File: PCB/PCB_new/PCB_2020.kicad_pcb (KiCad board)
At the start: 2 copper layers, 94 x 98.4 mm, 41 parts, among them IC1 LM358N, J1 SSW-110-02-G-S, J2 SSW-110-02-G-S, J3 SSW-110-02-G-S, J4 SSW-110-02-G-S, J5 SSW-110-02-G-S, J6 SSW-110-02-G-S, J7 SSW-110-02-G-S, J8 SSW-110-02-G-S, Q1 220mA/50V/3.5Ω, Q10 100V/17A, Q2 100V/17A, Q6 100V/17A, Q7 100V/17A, Q8 100V/17A, Q9 100V/17A

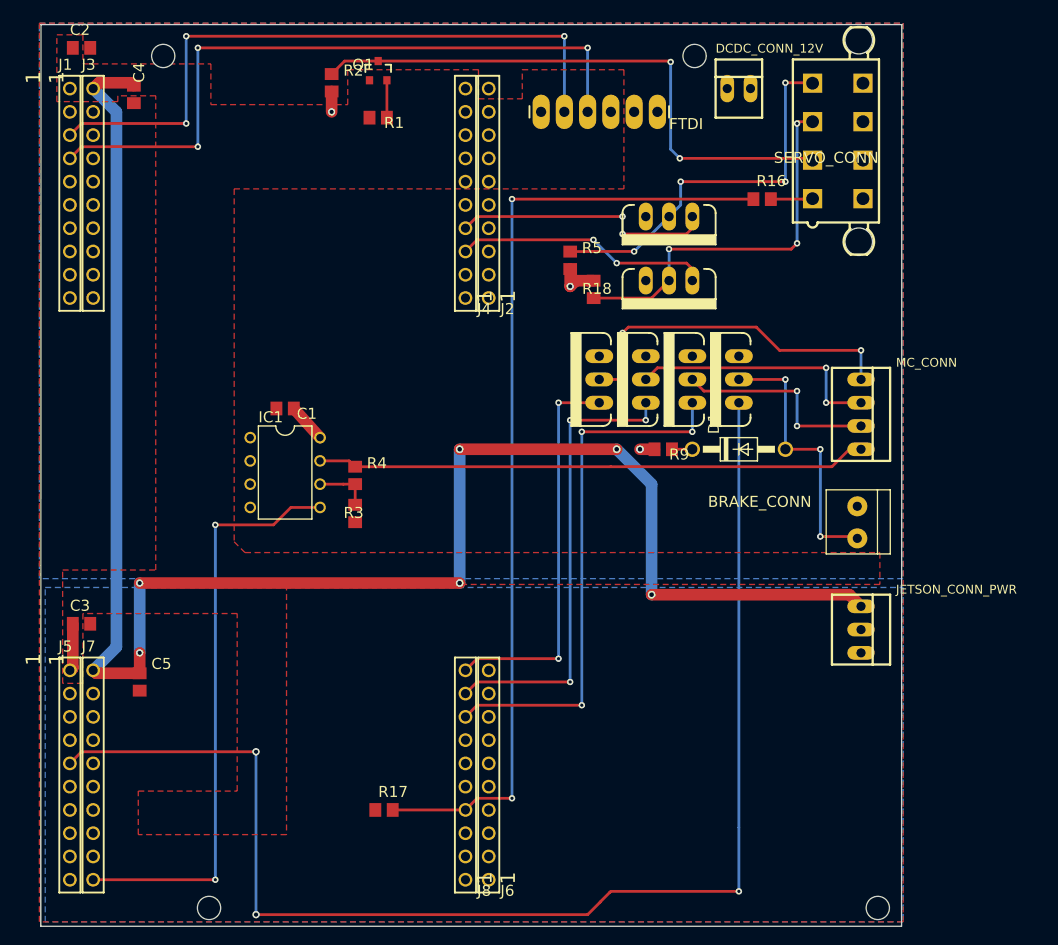
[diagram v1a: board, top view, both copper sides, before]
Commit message: tried to update PCB with new components but got weird results (not working)
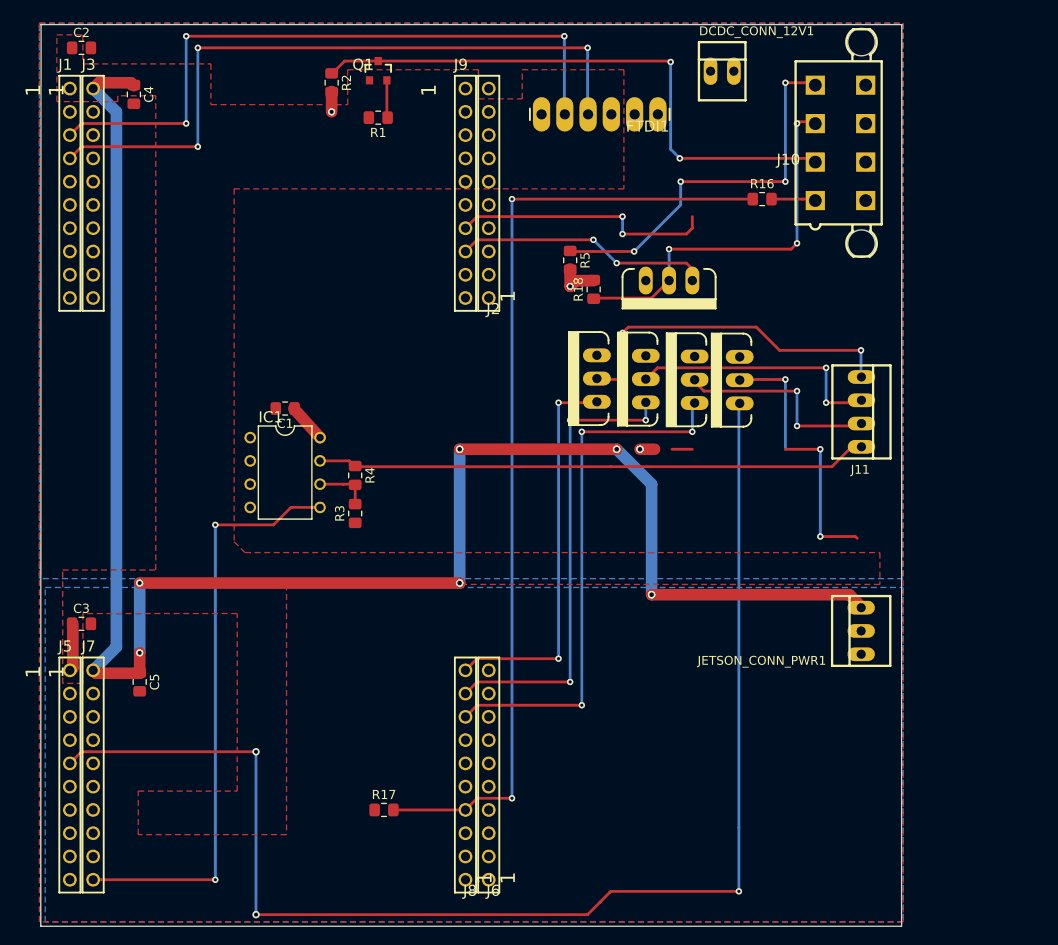
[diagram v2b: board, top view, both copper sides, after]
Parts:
- removed @HOLE0, @HOLE1, @HOLE2, @HOLE3: , 
- removed BRAKE_CONN: 1X2-3.5MM, 1X2-3.5MM
- removed D1: 1N4004, DO41-10
- removed DCDC_CONN_12V: 22-23-2021, 22-23-2021
- removed FTDI: , 1X06_LONGPADS
- removed J4: SSW-110-02-G-S, SSW-110-02-G-S
- removed JETSON_CONN_PWR: 22-23-2031, 22-23-2031
- removed MC_CONN: 22-23-2041, 22-23-2041
- removed Q10, Q7, Q8, Q9: 100V/17A, TO220V
- removed R9: , R0805
- removed SERVO_CONN: 5566-8, 5566-8
- added DCDC_CONN_12V1: 22-23-2021, Drivetrain_control:22-23-2021, F.Cu at (175.9, 60.9)
- added FTDI1: CONN_06LONGPADS, Drivetrain_control:1X06_LONGPADS, F.Cu at (168.9, 65.6)
- added J10: SERVO_CONN, Drivetrain_control:5566-8, F.Cu at (188.8, 68.7)
- added J11: MC_CONN, Drivetrain_control:22-23-2041, F.Cu at (191.1, 98.1)
- added J9: TI_BRR, Drivetrain_control:SSW-110-02-G-S, F.Cu at (147.9, 74.2)
- added JETSON_CONN_PWR1: 22-23-2031, Drivetrain_control:22-23-2031, F.Cu at (191.1, 122.0)
- added Q3: 100V/17A, Drivetrain_control:TO220V, F.Cu at (177.8, 94.6)
- added Q4: 100V/17A, Drivetrain_control:TO220V, F.Cu at (167.6, 94.5)
- added Q5: 100V/17A, Drivetrain_control:TO220V, F.Cu at (172.9, 94.6)
- C1, C2, C3, C4, C5: footprint C0805 -> Capacitor_SMD:C_0805_2012Metric_Pad1.15x1.40mm_HandSolder
- IC1: footprint DIL08 -> Drivetrain_control:DIL08
- J1: value SSW-110-02-G-S -> TI_TLL; footprint SSW-110-02-G-S -> Drivetrain_control:SSW-110-02-G-S
- J2: value SSW-110-02-G-S -> TI_BLL; footprint SSW-110-02-G-S -> Drivetrain_control:SSW-110-02-G-S
- J3: value SSW-110-02-G-S -> TI_BLR; footprint SSW-110-02-G-S -> Drivetrain_control:SSW-110-02-G-S
- J5: value SSW-110-02-G-S -> TI_TLR; footprint SSW-110-02-G-S -> Drivetrain_control:SSW-110-02-G-S
- J6: value SSW-110-02-G-S -> TI_BRL; footprint SSW-110-02-G-S -> Drivetrain_control:SSW-110-02-G-S
- J7: value SSW-110-02-G-S -> TI_TRL; footprint SSW-110-02-G-S -> Drivetrain_control:SSW-110-02-G-S
- J8: value SSW-110-02-G-S -> TI_TRR; footprint SSW-110-02-G-S -> Drivetrain_control:SSW-110-02-G-S
- Q1: footprint SOT23-3 -> Drivetrain_control:SOT23-3
- Q2, Q6: footprint TO220V -> Drivetrain_control:TO220V
- R1, R2: footprint R0805 -> Resistor_SMD:R_0805_2012Metric_Pad1.15x1.40mm_HandSolder
- R16, R17, R18, R3, R4, R5: value (none) -> R-US_R0805; footprint R0805 -> Resistor_SMD:R_0805_2012Metric_Pad1.15x1.40mm_HandSolder
- moved Q6 19.4 mm to (162.2, 94.4), turned to 90 degrees
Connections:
- IC1 pad 1: (no net) -> /LAUNCHXL-F28379D Breakout/THROTTLE_MC
- IC1 pad 2: (no net) -> Net-(IC1-Pad2)
- IC1 pad 3: (no net) -> THROTTLE_DAC
- IC1 pad 5: THROTTLE_DAC -> +12V
- IC1 pad 6: N$1 -> (no net)
- IC1 pad 7: THROTTLE_MC -> (no net)
- IC1 pad 8: +12V -> (no net)
- J1 pad 10: GPIO104/I2CSDAA/J1 -> (no net)
- J1 pad 2: GPIO32 -> (no net)
- J1 pad 5: GPIO67 -> (no net)
- J1 pad 6: GPIO111 -> (no net)
- J1 pad 7: GPIO60/SPICLKA -> (no net)
- J1 pad 8: GPIO22 -> (no net)
- J1 pad 9: GPIO105/I2SSCLA/J1 -> (no net)
- J2 pad 1: GPIO29/OPXBAR6 -> +3V3
- J2 pad 10: GND -> (no net)
- J2 pad 2: GPIO125/SD1CLK2 -> (no net)
- J2 pad 3: GPIO124/SD1D2 -> (no net)
- J2 pad 4: GPIO59/SPIAMISO -> (no net)
- J2 pad 5: GPIO58/SPIAMOSI -> (no net)
- J2 pad 6: RESET -> (no net)
- J2 pad 7: GPIO122/SD1D1 -> (no net)
- J2 pad 8: GPIO123/SD1CLK1 -> (no net)
- J2 pad 9: GPIO61/SPIACS -> (no net)
- J3 pad 10: ADCA0 -> THROTTLE_DAC
- J3 pad 3: ADCIN1 -> (no net)
- J3 pad 4: ADCINC3 -> (no net)
- J3 pad 5: ADCINB3 -> (no net)
- J3 pad 6: ADCINA3 -> (no net)
- J3 pad 7: ADCINC2 -> (no net)
- J3 pad 8: ADCINB2 -> (no net)
- J3 pad 9: ADCINA2 -> (no net)
- J5 pad 1: +3V3 -> +5V
- J5 pad 10: I2CSDAB -> (no net)
- J5 pad 2: FEATHER_RESET -> GND
- J5 pad 3: GPIO139/SCICRX(->MCU) -> (no net)
- J5 pad 4: GPIO56/SCICTX(<-MCU) -> (no net)
- J5 pad 5: KILL_SIGNAL -> (no net)
- J5 pad 6: GPIO94 -> (no net)
- J5 pad 7: GPIO65/SPIBCLK -> (no net)
- J5 pad 8: GPIO52/J5 -> (no net)
- J5 pad 9: I2CSCLB -> (no net)
- J6 pad 1: GPIO25/OPXBAR2 -> FS1_CTL
- J6 pad 10: GND -> (no net)
- J6 pad 2: GPIO27/SD2CLK2 -> FWD_CTL
- J6 pad 3: GPIO26/SD2D2 -> REV_CTL
- J6 pad 4: GPIO64/SPIBMISO -> (no net)
- J6 pad 5: GPIO63/SPIBMOSI -> (no net)
- J6 pad 6: RESET -> (no net)
- J6 pad 7: GPIO130/SD2D1 -> MC_HLFB+
- J6 pad 8: GPIO131/SD2CLK1 -> (no net)
- J6 pad 9: GPIO66/SPIBCS -> (no net)
- J7 pad 1: +5V -> TI_PWM
- J7 pad 10: THROTTLE_DAC -> (no net)
- J7 pad 2: GND -> (no net)
- J7 pad 3: ADCIN15 -> (no net)
- J7 pad 4: ADCINC5 -> (no net)
- J7 pad 5: ADCINB5 -> (no net)
- J7 pad 6: ADCINA5 -> (no net)
- J7 pad 7: ADCINC4 -> EN+_CTL
- J7 pad 8: ADCINB4 -> INPUT_A+_CTL
- J7 pad 9: ADCINA4 -> (no net)
- J8 pad 1: PWM/BASED/DAC4 -> GND
- J8 pad 10: FS1_CTL -> (no net)
- J8 pad 2: PWM/BASED/DAC3 -> (no net)
- J8 pad 3: GPIO15/OPXBAR4 -> (no net)
- J8 pad 4: MC_HLFB+ -> (no net)
- J8 pad 5: MC_W -> /LAUNCHXL-F28379D Headers/RESET
- J8 pad 6: MC_V -> (no net)
- J8 pad 7: MC_U -> (no net)
- J8 pad 8: REV_CTL -> (no net)
- J8 pad 9: FWD_CTL -> (no net)
- Q1 pad 1: +3V3 -> /LAUNCHXL-F28379D Breakout/INPUT_B+
- Q1 pad 2: TI_PWM -> +3V3
- Q1 pad 3: INPUT_B+ -> TI_PWM
- Q2 pad 1: INPUT_A+_CTL -> /LAUNCHXL-F28379D Breakout/INPUT_A+
- Q2 pad 2: INPUT_A+ -> INPUT_A+_CTL
- Q6 pad 1: EN+_CTL -> /LAUNCHXL-F28379D Breakout/FS1_MC
- Q6 pad 2: EN+ -> FS1_CTL
- R1 pad 1: TI_PWM -> +3V3
- R1 pad 2: +3V3 -> TI_PWM
- R16 pad 1: MC_HLFB+ -> /LAUNCHXL-F28379D Breakout/HLFB+
- R16 pad 2: HLFB+ -> MC_HLFB+
- R17 pad 1: GND -> MC_HLFB+
- R17 pad 2: MC_HLFB+ -> GND
- R18 pad 1: INPUT_A+ -> +12V
- R18 pad 2: +12V -> /LAUNCHXL-F28379D Breakout/INPUT_A+
- R2 pad 1: INPUT_B+ -> +12V
- R2 pad 2: +12V -> /LAUNCHXL-F28379D Breakout/INPUT_B+
- R3 pad 1: GND -> Net-(IC1-Pad2)
- R3 pad 2: N$1 -> GND
- R4 pad 1: THROTTLE_MC -> Net-(IC1-Pad2)
- R4 pad 2: N$1 -> /LAUNCHXL-F28379D Breakout/THROTTLE_MC
- R5 pad 1: EN+ -> +12V
- R5 pad 2: +12V -> /LAUNCHXL-F28379D Breakout/EN+
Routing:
- net (no net): track 0.00 -> 326.5 mm, vias 0 -> 13
- net KILL_SIGNAL: track 145.7 -> 0.00 mm, vias 3 -> 0
- net REV_CTL: track 58.3 -> 0.00 mm, vias 3 -> 0
- net FWD_CTL: track 50.7 -> 0.00 mm, vias 3 -> 0
- net FS1_CTL: track 43.1 -> 0.00 mm, vias 2 -> 0
- net FS1_MC: track 38.1 -> 0.00 mm, vias 3 -> 0
- net /LAUNCHXL-F28379D Breakout/THROTTLE_MC: track 0.00 -> 38.1 mm, vias 0 -> 3
- net INPUT_A+_CTL: track 27.9 -> 0.00 mm, vias 2 -> 0
- net /LAUNCHXL-F28379D Breakout/INPUT_A+: track 0.00 -> 27.9 mm, vias 0 -> 2
- net FWD_MC: track 27.8 -> 0.00 mm, vias 2 -> 0
- net /LAUNCHXL-F28379D Breakout/REV_MC: track 0.00 -> 27.8 mm, vias 0 -> 2
- net REV_MC: track 22.8 -> 0.00 mm, vias 2 -> 0
- net /LAUNCHXL-F28379D Breakout/FWD_MC: track 0.00 -> 22.8 mm, vias 0 -> 2
- net EN+_CTL: track 28.7 -> 12.7 mm, vias 2 -> 1
- net BRAKE_SOLENOID: track 30.1 -> 17.4 mm, vias 3 -> 2
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
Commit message: fixed mosfet pins, realized TI pins incorrect orientation
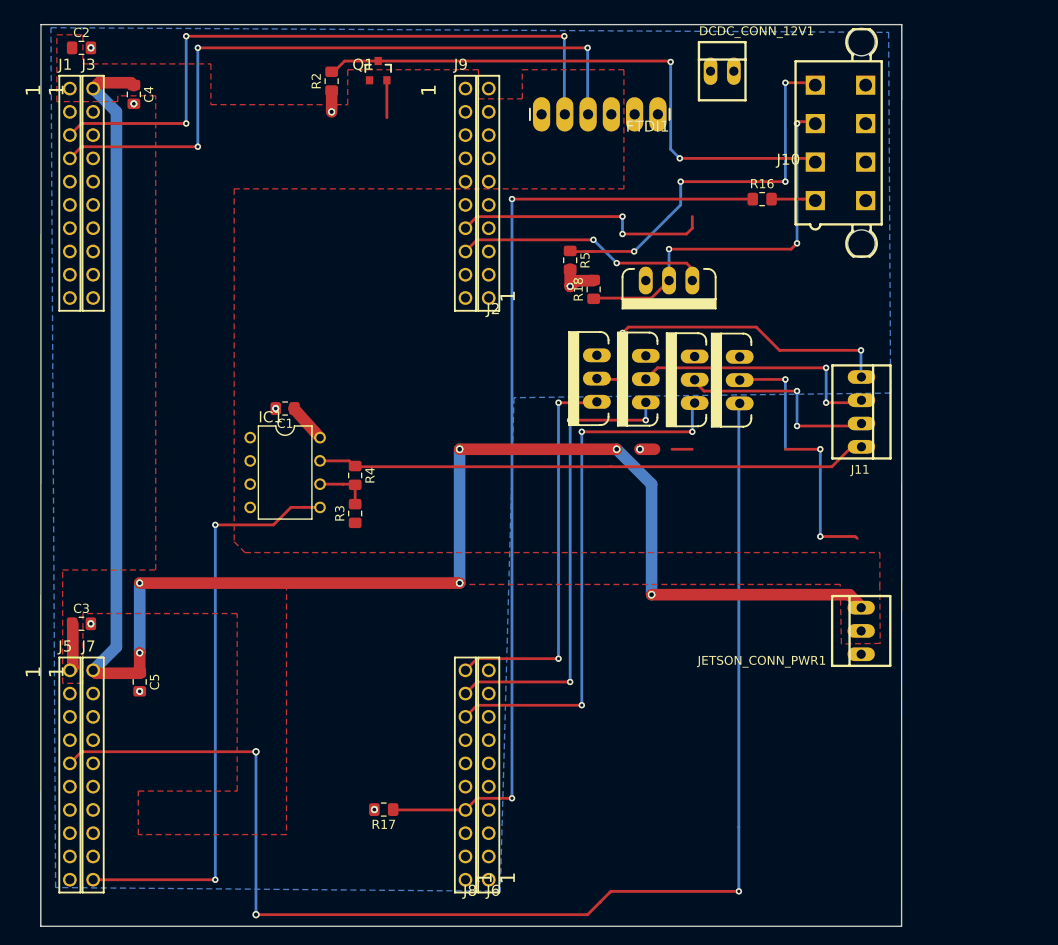
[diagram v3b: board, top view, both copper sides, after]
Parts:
- removed R1: 10k, Resistor_SMD:R_0805_2012Metric_Pad1.15x1.40mm_HandSolder
- Q1: footprint Drivetrain_control:SOT23-3 -> Drive_Train_Control:SOT23-3
- moved R2 0.17 mm to (133.3, 62.0), turned to 90 degrees
- turned R17 to 180 degrees
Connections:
- Q1 pad 1: /LAUNCHXL-F28379D Breakout/INPUT_B+ -> +3V3
- Q1 pad 2: +3V3 -> TI_PWM
- Q1 pad 3: TI_PWM -> /LAUNCHXL-F28379D Breakout/INPUT_B+
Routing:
- net INPUT_B+: track 63.1 -> 0.00 mm, vias 2 -> 0
- net /LAUNCHXL-F28379D Breakout/INPUT_B+: track 2.22 -> 63.1 mm, vias 1 -> 2
- net TI_PWM: track 0.00 -> 4.08 mm
- net +3V3: track 9.34 -> 5.26 mm
- net +12V: track 10.6 -> 12.8 mm, vias 2 -> 3
- net GND: vias 0 -> 6
- added copper zone on B.Cu, net GND
- removed copper zone on B.Cu, net +12V
- removed copper zone on B.Cu, net +3V3
- removed copper zone on F.Cu, net GND

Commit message: Created TI schematic and Footprint
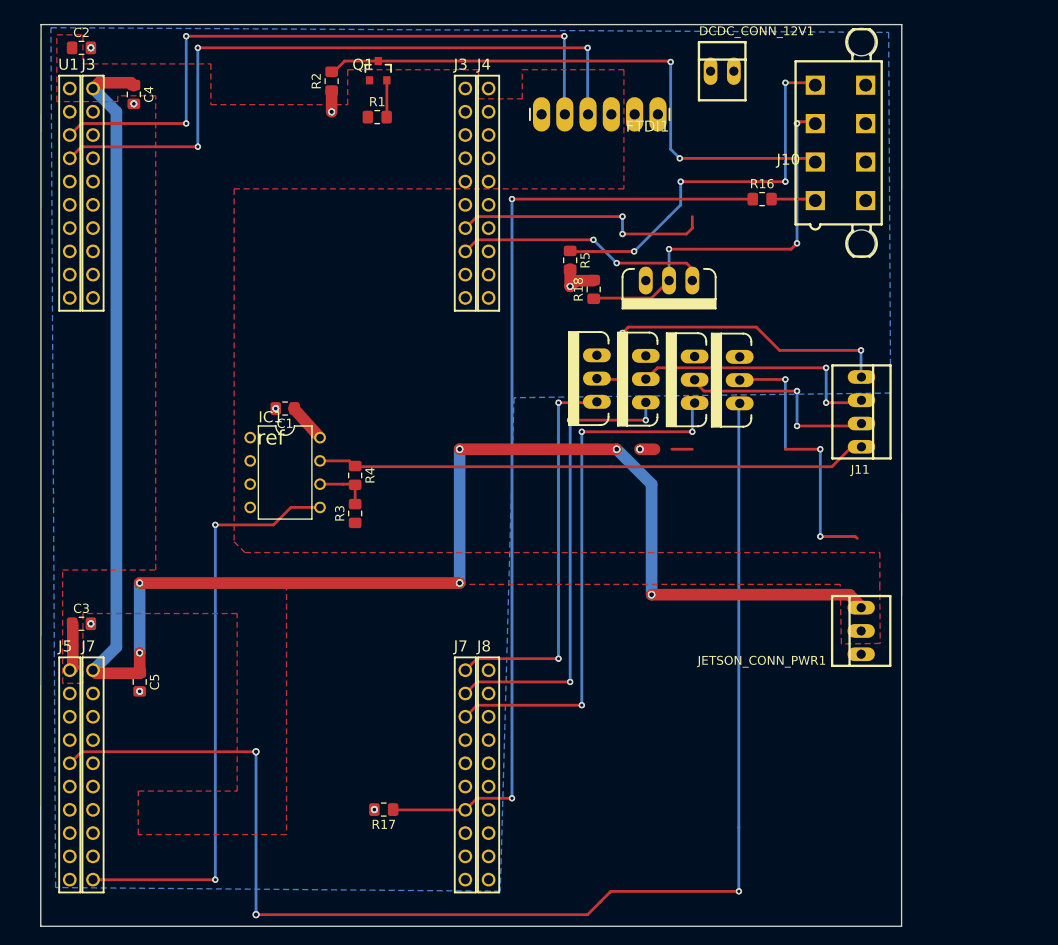
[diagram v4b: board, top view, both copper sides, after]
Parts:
- removed J1: TI_TLL, Drivetrain_control:SSW-110-02-G-S
- removed J2: TI_BLL, Drivetrain_control:SSW-110-02-G-S
- removed J3: TI_BLR, Drivetrain_control:SSW-110-02-G-S
- removed J5: TI_TLR, Drivetrain_control:SSW-110-02-G-S
- removed J6: TI_BRL, Drivetrain_control:SSW-110-02-G-S
- removed J7: TI_TRL, Drivetrain_control:SSW-110-02-G-S
- removed J8: TI_TRR, Drivetrain_control:SSW-110-02-G-S
- removed J9: TI_BRR, Drivetrain_control:SSW-110-02-G-S
- added R1: 10k, Resistor_SMD:R_0805_2012Metric_Pad1.15x1.40mm_HandSolder, F.Cu at (138.2, 65.9)
- added U1: TI_CONN, Drivetrain_control:TI_Footprint, F.Cu at (103.5, 87.0)
- Q1: footprint Drive_Train_Control:SOT23-3 -> Drivetrain_control:SOT23-3
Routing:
- net (no net): track 326.5 -> 0.00 mm, vias 13 -> 0
- net /LAUNCHXL-F28379D Breakout/EN+: track 0.00 -> 145.7 mm, vias 0 -> 3
- net THROTTLE_DAC: track 64.3 -> 0.00 mm, vias 2 -> 0
- net +12V: track 12.8 -> 77.1 mm, vias 3 -> 5
- net /LAUNCHXL-F28379D Breakout/FWD_MC: track 22.8 -> 81.1 mm, vias 2 -> 5
- net /LAUNCHXL-F28379D Breakout/REV_MC: track 27.8 -> 78.5 mm, vias 2 -> 5
- net /LAUNCHXL-F28379D Breakout/FS1_MC: track 0.00 -> 43.1 mm, vias 0 -> 2
- net EN+_CTL: track 12.7 -> 41.4 mm, vias 1 -> 3
